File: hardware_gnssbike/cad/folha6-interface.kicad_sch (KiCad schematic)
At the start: 23 parts, among them Q601 DMG1012T-7, Q602 DMG1012T-7, Q603 DMG1012T-7, SW601 XunPu TS-1088R-02026, SW602 XunPu TS-1088R-02026, SW603 XunPu TS-1088R-02026

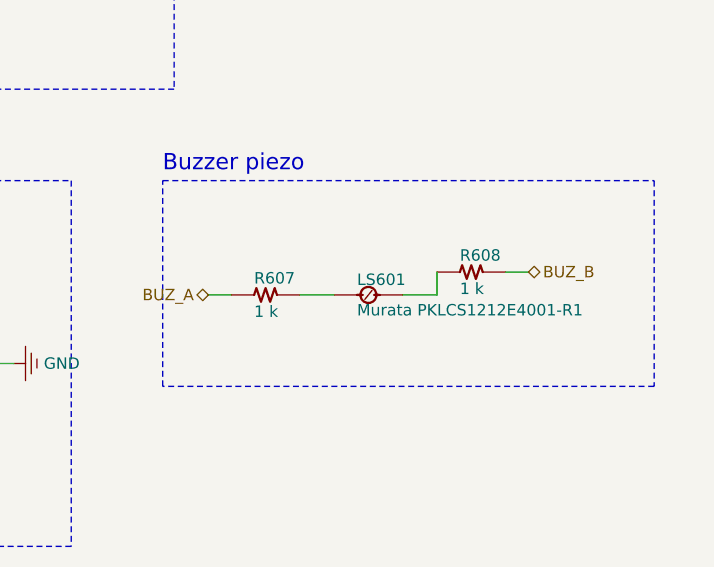
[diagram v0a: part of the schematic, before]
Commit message: feat(hardware): apply the schematic review, take either display, review the case
Apply the corrections the owner approved on 2026-10-18, in the
generators: the BMP585 land from figure 29, the RGB LED land unmirrored,
the TLV7031DCKR renumbered and fed from VBAT_SYS, the common pad of
JP301 in the middle, the OPT3001 exposed pad, the Murata land for the
buck inductors, 10 uF on PVDD and 3V3BL, a 24 V TVS on VBUS, the flash
on 3V0, pin-1 marks, the charge LEDs in the key row, the TVS next to
their connectors, the USB-C on the maker's edge line, the Same Sky
buzzer in place of the last-time-buy Murata, and an LCSC code on every
fitted part.

The board takes the JDI or the Sharp on one dual-contact Molex 503480:
JP401 picks 3V0 or 5V0, and a TPS610997 boost feeds the Sharp. A second
blind check found the connector drawn backwards (the tail enters on the
nail side); the land, the circuit order and the boost placement follow
the drawings now.

The router finds its way further: unique UUIDs per footprint, so the
DRC names the right pads; the chip antenna's own nets inside its
keep-out; JP301 turned so the two RF lines do not cross; ground vias
outside the dense chips, bent and geometrically checked ground stubs,
and a pass with the power rails first. The DRC reports no error; 60
items are still unconnected.

The case is reviewed part by part (hardware_gnssbike/12): the solar
module pockets follow the datasheet's +-0.3 mm (the case grows to 64 mm),
the keys stop 0.15 mm under the membrane, and the light sensor gets a
sealed window. The sealing of the USB-C, the floor holes and the lid
seam is left to the owner. The documents follow parts.py.

Nothing is fabricated, and the routing is still open.
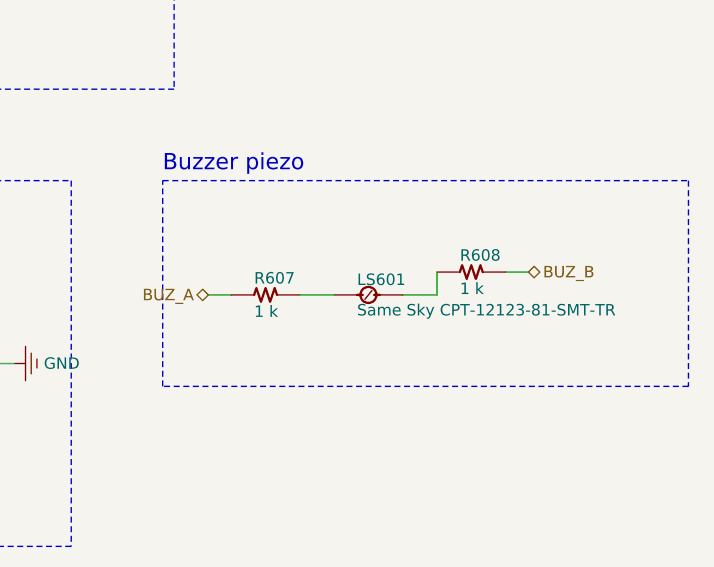
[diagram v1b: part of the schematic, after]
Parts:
- LS601: value Murata PKLCS1212E4001-R1 -> Same Sky CPT-12123-81-SMT-TR; footprint gnssbike:Buzzer_PKLCS1212E4001_12x12mm -> gnssbike:Buzzer_CPT-12123-81-SMT_12x12mm
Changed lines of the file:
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@@
 	(rectangle
 		(start 149.860 90.170)
-		(end 204.470 113.030)
+		(end 208.280 113.030)
 		(stroke (width 0.1524) (type dash))
 		(fill (type none))
@@
 			(effects (font (size 1.27 1.27)) (hide yes))
 		)
-		(property "Description" "chave de canal N de uma cor do LED; a Diodes nao publica numero de pino, a numeracao vem do padrao SOT-523 | PINAGEM NAO CONFIRMADA NA FICHA"
+		(property "Description" "chave de canal N de uma cor do LED; a Diodes nao publica numero de pino, a numeracao vem do padrao SOT-523"
 			(at 97.79 46.99 0)
 			(effects (font (size 1.27 1.27)) (hide yes))
@@
 			(effects (font (size 1.27 1.27)) (hide yes))
 		)
-		(property "Description" "chave de canal N de uma cor do LED; a Diodes nao publica numero de pino, a numeracao vem do padrao SOT-523 | PINAGEM NAO CONFIRMADA NA FICHA"
+		(property "Description" "chave de canal N de uma cor do LED; a Diodes nao publica numero de pino, a numeracao vem do padrao SOT-523"
 			(at 118.11 46.99 0)
 			(effects (font (size 1.27 1.27)) (hide yes))
@@
 			(effects (font (size 1.27 1.27)) (hide yes))
 		)
-		(property "Description" "chave de canal N de uma cor do LED; a Diodes nao publica numero de pino, a numeracao vem do padrao SOT-523 | PINAGEM NAO CONFIRMADA NA FICHA"
+		(property "Description" "chave de canal N de uma cor do LED; a Diodes nao publica numero de pino, a numeracao vem do padrao SOT-523"
 			(at 138.43 46.99 0)
 			(effects (font (size 1.27 1.27)) (hide yes))
@@
 			(effects (font (size 1.27 1.27)) (hide yes))
 		)
-		(property "Description" "Schottky que isola o P1.27 do no da tecla central; catodo no no, anodo no MCU. SOD-323; catodo no terminal 1 CONFERIR pela marca | PINAGEM NAO CONFIRMADA NA FICHA"
+		(property "Description" "Schottky que isola o P1.27 do no da tecla central; catodo no no, anodo no MCU. SOD-323; catodo no terminal 1, conferido na revisao de 2026-10-18"
 			(at 66.04 100.33 0)
 			(effects (font (size 1.27 1.27)) (hide yes))
@@
 			(effects (font (size 1.27 1.27)) (justify left bottom))
 		)
-		(property "Value" "Murata PKLCS1212E4001-R1"
+		(property "Value" "Same Sky CPT-12123-81-SMT-TR"
 			(at 171.450 103.820 0)
 			(effects (font (size 1.27 1.27)) (justify left top))
 		)
-		(property "Footprint" "gnssbike:Buzzer_PKLCS1212E4001_12x12mm"
+		(property "Footprint" "gnssbike:Buzzer_CPT-12123-81-SMT_12x12mm"
 			(at 172.72 102.87 0)
 			(effects (font (size 1.27 1.27)) (hide yes))
@@
 			(effects (font (size 1.27 1.27)) (hide yes))
 		)
-		(property "Description" "buzzer piezo passivo, 12 x 12 x 3,0 mm, 84 dB a 4 kHz, acionado em contrafase. Sem polaridade. Furo de som LATERAL, rente a placa"
+		(property "Description" "buzzer piezo passivo, 12 x 12 x 3,0 mm, 81 dB a 4 kHz, acionado em contrafase. Sem polaridade. Furo de som LATERAL"
 			(at 172.72 102.87 0)
 			(effects (font (size 1.27 1.27)) (hide yes))
